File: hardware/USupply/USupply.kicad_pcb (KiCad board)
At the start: 2 copper layers, 11 parts, among them P1 USB_C_Receptacle_USB2.0, Q1 Si2319CDS, U1 HUSB238

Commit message: refactor(hw/usb): refine usb pd by sub
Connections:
- net /Gate renamed /USB_PD/Gate
- net VDD renamed VDC
- C1 pad 1: VBUS -> Net-(U1-VIN)
- P1 pad A4: +VDC -> VBUS
- P1 pad A9: +VDC -> VBUS
- P1 pad B4: +VDC -> VBUS
- P1 pad B9: +VDC -> VBUS
- Q1 pad 2: +VDC -> VBUS
- R1 pad 1: +VDC -> VBUS
- R1 pad 2: VBUS -> Net-(U1-VIN)
- R3 pad 2: +VDC -> VBUS
- U1 pad 1: VBUS -> Net-(U1-VIN)
- U1 pad 6: unconnected-(U1-SDA-Pad6) -> /USB_PD/I2C_SDA
- U1 pad 7: unconnected-(U1-SCL-Pad7) -> /USB_PD/I2C_SCL
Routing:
- net VBUS: track 0.00 -> 7.97 mm
- net +VDC: track 7.97 -> 0.00 mm

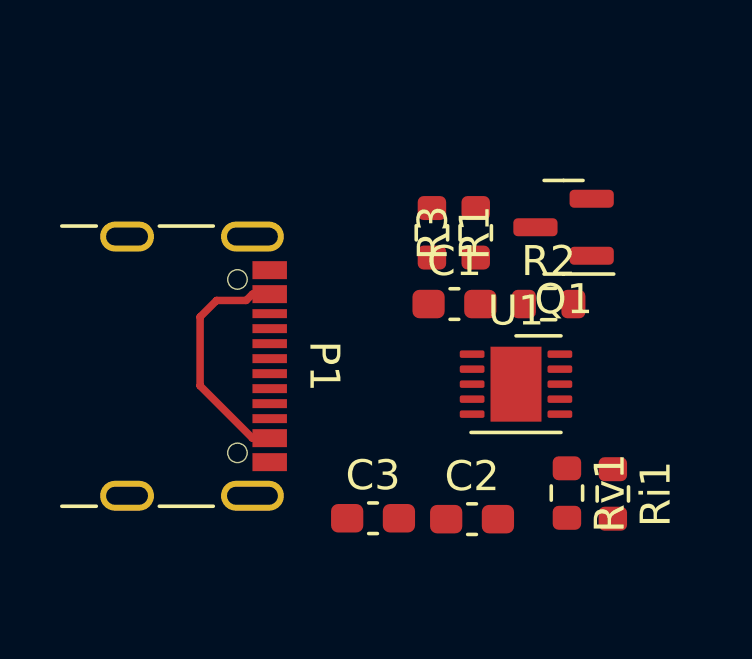
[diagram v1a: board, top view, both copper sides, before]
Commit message: feat(hw/usb): update usb pd circuit
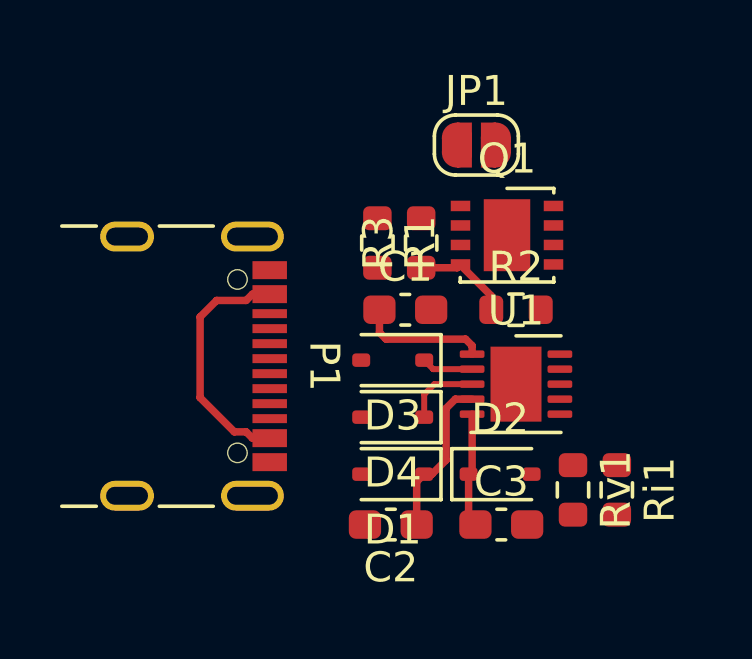
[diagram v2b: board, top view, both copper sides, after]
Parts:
- added D1: TVS, Diode_SMD:D_SOD-323, F.Cu at (63.1, 94.0)
- added D2: TVS, Diode_SMD:D_SOD-323, F.Cu at (66.7, 94.0)
- added D3: TVS, Diode_SMD:D_SOD-323, F.Cu at (63.1, 90.2)
- added D4: TVS, Diode_SMD:D_SOD-323, F.Cu at (63.1, 92.1)
- added JP1: Jumper_2_Open, Jumper:SolderJumper-2_P1.3mm_Open_RoundedPad1.0x1.5mm, F.Cu at (65.9, 83.1)
- Q1: value Si2319CDS -> AGM30P08AP; footprint Package_TO_SOT_SMD:SOT-23 -> Package_DFN_QFN:DFN-8-1EP_3x3mm_P0.65mm_EP1.55x2.4mm
- moved C3 4.28 mm to (66.8, 95.7)
- moved C2 2.71 mm to (63.1, 95.7), turned to 180 degrees
- moved Q1 1.90 mm to (66.9, 86.1), turned to 0 degrees
- moved R1 1.85 mm to (62.6, 86.3)
- moved R3 1.85 mm to (64.1, 86.3)
- moved C1 1.65 mm to (63.5, 88.6)
- moved R2 1.10 mm to (67.2, 88.6)
- moved Rv1 0.23 mm to (69.1, 94.6)
- moved Ri1 0.19 mm to (70.6, 94.6)
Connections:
- Q1 pad 1: Net-(Q1-G) -> VBUS
- Q1 pad 3: VDC -> VBUS
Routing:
- net /CC1: track 0.00 -> 5.43 mm
- net Net-(U1-VIN): track 0.00 -> 4.31 mm
- net /CC2: track 0.00 -> 3.82 mm
- net Net-(Q1-G): track 0.00 -> 3.29 mm
- net /D-: track 0.00 -> 2.50 mm
- net /D+: track 0.00 -> 1.72 mm
